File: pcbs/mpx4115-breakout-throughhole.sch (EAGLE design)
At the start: 5 parts

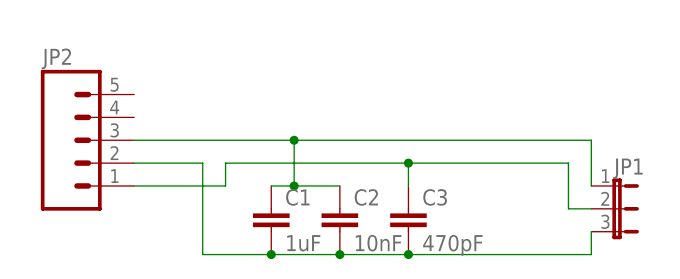
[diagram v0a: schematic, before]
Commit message: now with 6 holes for pressure sensor
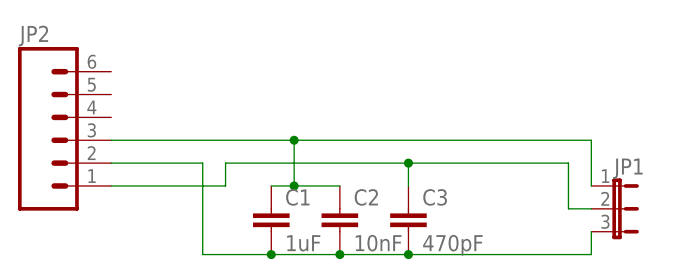
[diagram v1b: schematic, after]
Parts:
- JP2: device SparkFun-Connectors:M05PTH -> SparkFun-Connectors:M06NO_SILK
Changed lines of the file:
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@@
 <part name="C2" library="resistor" deviceset="C-EU" device="C0805" value="10nF"/>
 <part name="C3" library="resistor" deviceset="C-EU" device="C0805" value="470pF"/>
-<part name="JP2" library="SparkFun-Connectors" deviceset="M05" device="PTH"/>
+<part name="JP2" library="SparkFun-Connectors" deviceset="M06" device="NO_SILK"/>
 </parts>
 <sheets>
@@
 <pinref part="C3" gate="G$1" pin="2"/>
 <pinref part="JP2" gate="G$1" pin="2"/>
-<wire x1="10.16" y1="25.4" x2="17.78" y2="25.4" width="0.1524" layer="91"/>
+<wire x1="7.62" y1="25.4" x2="17.78" y2="25.4" width="0.1524" layer="91"/>
 <wire x1="17.78" y1="25.4" x2="17.78" y2="15.24" width="0.1524" layer="91"/>
 <wire x1="17.78" y1="15.24" x2="25.4" y2="15.24" width="0.1524" layer="91"/>
@@
 <pinref part="JP2" gate="G$1" pin="3"/>
 <wire x1="60.96" y1="27.94" x2="60.96" y2="22.86" width="0.1524" layer="91"/>
-<wire x1="10.16" y1="27.94" x2="27.94" y2="27.94" width="0.1524" layer="91"/>
+<wire x1="7.62" y1="27.94" x2="27.94" y2="27.94" width="0.1524" layer="91"/>
 <pinref part="C1" gate="G$1" pin="1"/>
 <pinref part="C2" gate="G$1" pin="1"/>
@@
 <wire x1="40.64" y1="25.4" x2="40.64" y2="22.86" width="0.1524" layer="91"/>
 <pinref part="JP2" gate="G$1" pin="1"/>
-<wire x1="10.16" y1="22.86" x2="20.32" y2="22.86" width="0.1524" layer="91"/>
+<wire x1="7.62" y1="22.86" x2="20.32" y2="22.86" width="0.1524" layer="91"/>
 <wire x1="20.32" y1="22.86" x2="20.32" y2="25.4" width="0.1524" layer="91"/>
 <wire x1="20.32" y1="25.4" x2="40.64" y2="25.4" width="0.1524" layer="91"/>
